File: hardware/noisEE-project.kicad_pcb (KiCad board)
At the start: 2 copper layers, 109.9 x 56.5 mm, 113 parts, among them IC1 ATTINY84-S, J1 VOL_CONN, J2 Stereo_CONN, J3 COLOR_CONN, J4 USB_OTG, M3 MountingHole_3.2mm_M3, P2 ISP_02x03, Q1 PN2222A, Q2 PN2222A, SW1 SW_DIP_x01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

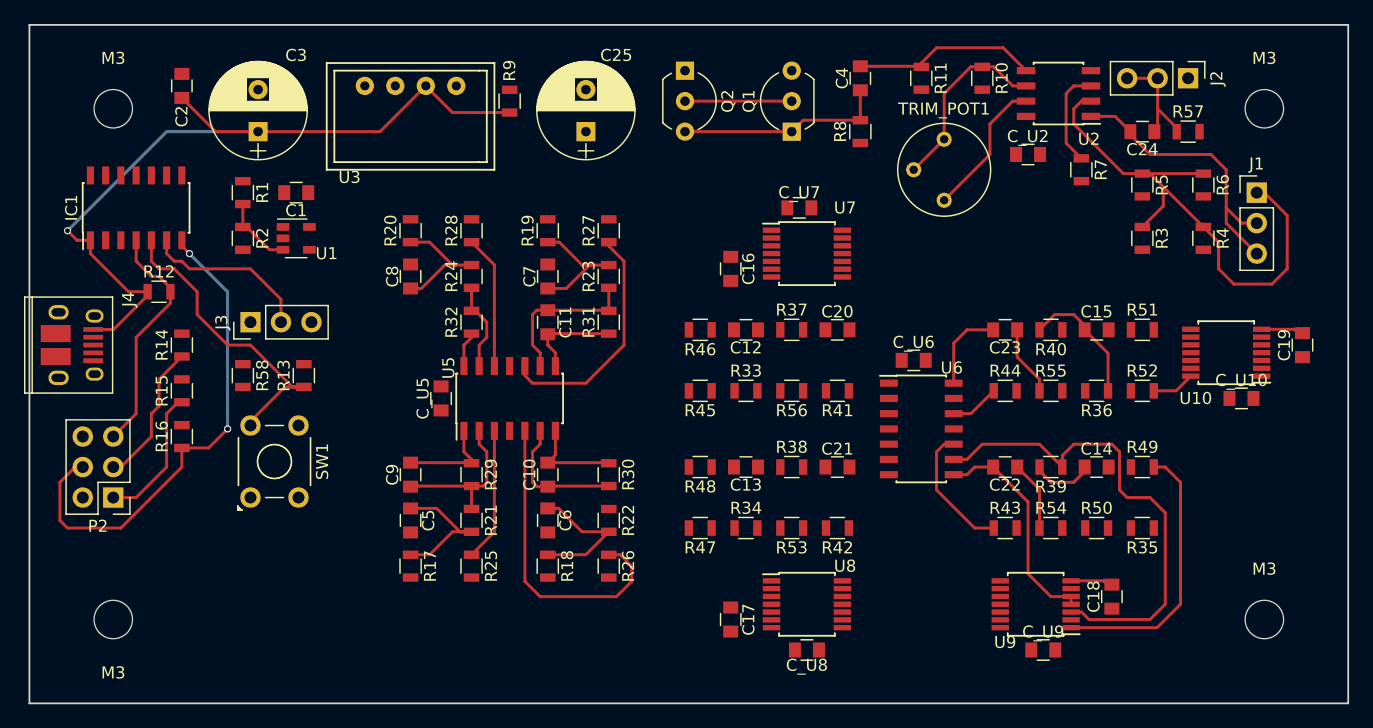
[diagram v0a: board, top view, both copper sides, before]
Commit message: Use two opamps for pre-amp and output stages, clean up board and lay down tracks for all signal paths
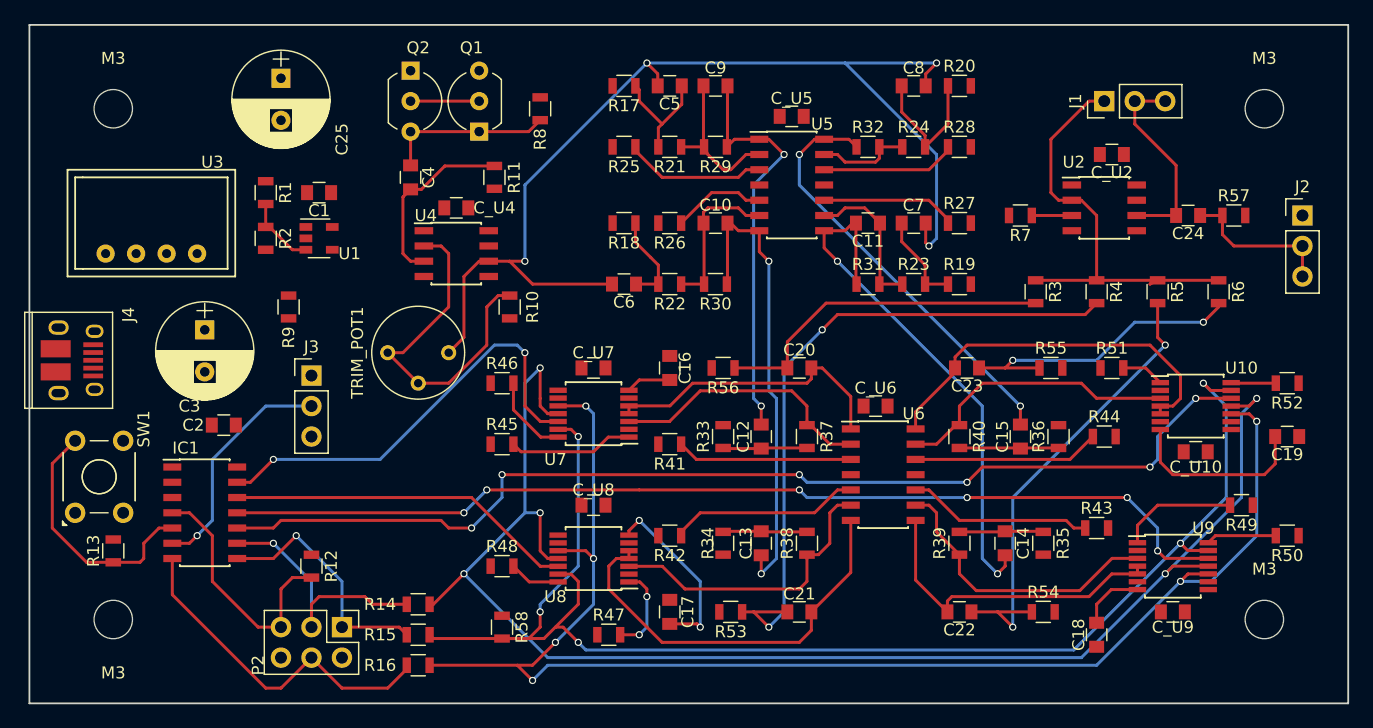
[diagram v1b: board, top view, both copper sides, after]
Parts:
- added C_U4: 0.1u, Capacitors_SMD:C_0805, F.Cu at (102.9, 74.9)
- added U4: OPA227, Housings_SOIC:SOIC-8_3.9x4.9mm_Pitch1.27mm, F.Cu at (102.9, 78.7)
- U2: value OPA2227 -> OPA227
- moved R20 47.3 mm to (144.8, 64.8), turned to 0 degrees
- moved C8 44.8 mm to (141.0, 64.8), turned to 0 degrees
- moved R17 43.8 mm to (116.8, 64.8), turned to 180 degrees
- moved R10 43.7 mm to (107.3, 83.2)
- moved TRIM_POT1 43.2 mm to (102.2, 87.0), turned to 90 degrees
- moved C5 42.1 mm to (120.7, 64.8), turned to 180 degrees
- moved R28 41.2 mm to (144.8, 69.8), turned to 0 degrees
- moved C9 41.2 mm to (124.5, 64.8), turned to 0 degrees
- moved R24 38.4 mm to (141.0, 69.8), turned to 0 degrees
- moved C4 38.4 mm to (99.1, 72.4), turned to 270 degrees
- moved C_U5 37.5 mm to (130.8, 67.3), turned to 0 degrees
- moved R25 37.2 mm to (116.8, 69.8), turned to 180 degrees
- moved R11 36.5 mm to (106.0, 72.4)
- moved R32 36.1 mm to (137.2, 69.8), turned to 0 degrees
- moved R21 35.2 mm to (120.7, 69.8), turned to 180 degrees
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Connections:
- U2 pad 1: Net-(C24-Pad2) -> Net-(U2-Pad1)
- U2 pad 5: Net-(C4-Pad2) -> Net-(U2-Pad5)
- U2 pad 6: Net-(R10-Pad1) -> Net-(C24-Pad2)
- U2 pad 7: Noise -> +9V
- U2 pad 8: +9V -> Net-(U2-Pad8)
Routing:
- net SPI_CLK: track 0.00 -> 123.0 mm, vias 0 -> 5
- net SPI_MOSI: track 0.00 -> 119.7 mm, vias 0 -> 6
- net SPI_MISO: track 0.00 -> 117.6 mm, vias 0 -> 5
- net SS_INFT: track 0.00 -> 90.6 mm, vias 0 -> 6
- net SS_5300: track 0.00 -> 85.2 mm, vias 0 -> 6
- net Noise: track 11.7 -> 91.9 mm, vias 0 -> 4
- net +5V: track 65.7 -> 0.00 mm, vias 1 -> 0
- net N_0270: track 0.00 -> 55.9 mm, vias 0 -> 2
- net SS_0016: track 0.00 -> 36.7 mm, vias 0 -> 2
- net Net-(C11-Pad2): track 8.01 -> 44.4 mm, vias 0 -> 2
- net W_0270: track 0.00 -> 34.1 mm
- net N_5300: track 5.85 -> 39.3 mm, vias 0 -> 2
- net Net-(C15-Pad2): track 2.96 -> 35.7 mm, vias 0 -> 2
- net Net-(C10-Pad2): track 8.01 -> 39.2 mm, vias 0 -> 2
- net SS_0270: track 0.00 -> 29.1 mm
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
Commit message: Laid down almost all tracks. GND and Earth seem to be treated as synonyms
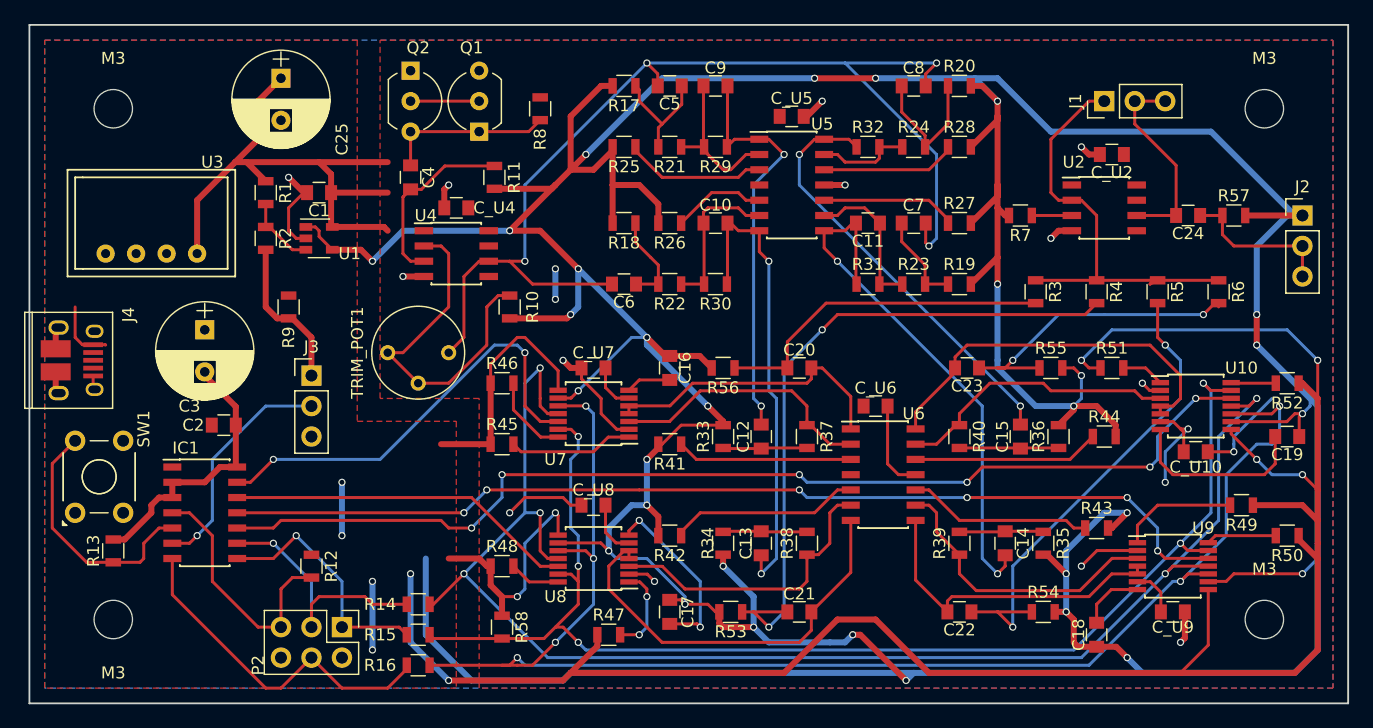
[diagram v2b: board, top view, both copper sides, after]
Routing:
- net GND: track 0.00 -> 476.3 mm, vias 0 -> 30
- net +5V: track 0.00 -> 212.5 mm, vias 0 -> 8
- net Earth: track 0.00 -> 103.0 mm, vias 0 -> 14
- net +9V: track 0.00 -> 70.1 mm, vias 0 -> 2
- net (no net): track 0.00 -> 12.7 mm, vias 0 -> 6
- net SPI_MISO: track 117.6 -> 108.4 mm
- net SPI_MOSI: track 119.7 -> 123.7 mm
- net N_5300: track 39.3 -> 40.4 mm
- net N_INFT: track 25.2 -> 26.0 mm
- added copper zone on F.Cu, net +5V
- added copper zone on F.Cu, net +9V
- added copper zone on B.Cu, net Earth

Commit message: Split up the ground (GND->VCOM)
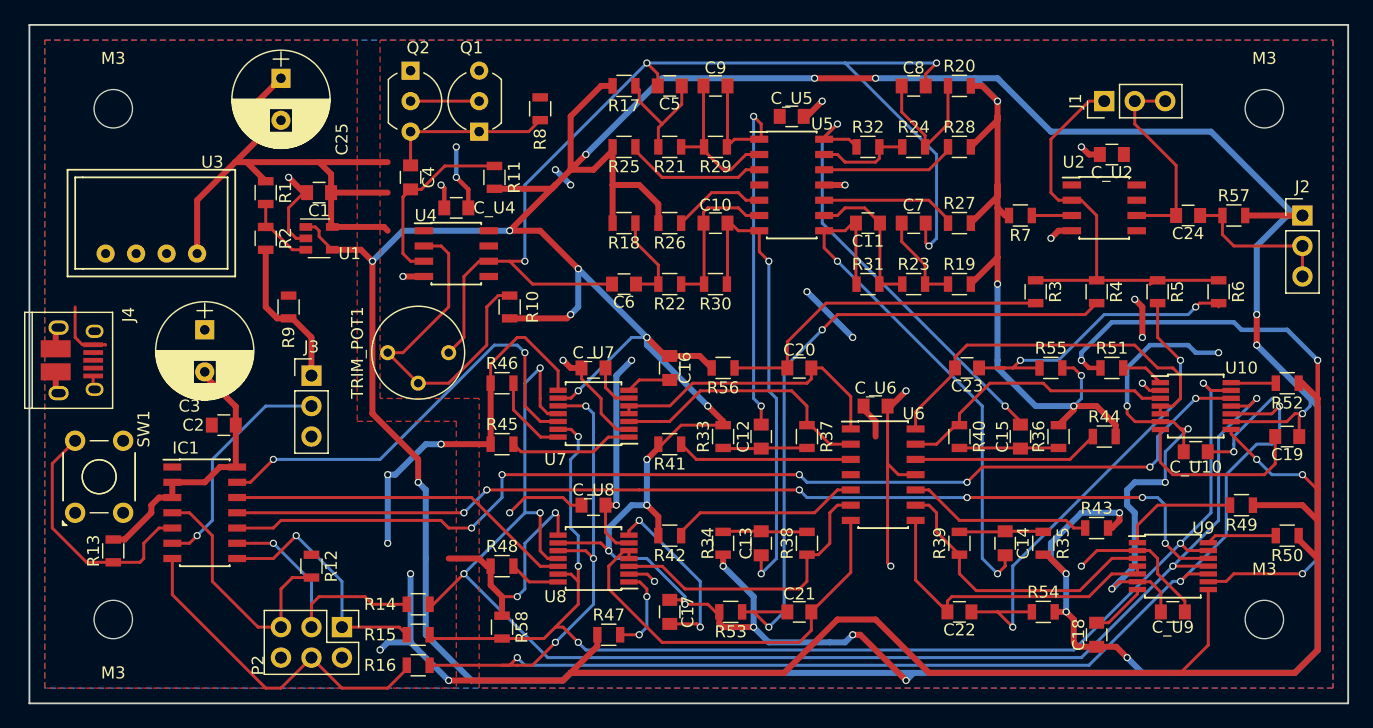
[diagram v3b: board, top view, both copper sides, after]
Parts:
- C4: value 1uF -> 1u
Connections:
- net GND renamed VCOM
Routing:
- net +9V: track 70.1 -> 129.8 mm, vias 2 -> 13
- net VCOM: track 476.3 -> 504.1 mm, vias 30 -> 31
- net Earth: track 103.0 -> 121.7 mm, vias 14 -> 17
- net +5V: track 212.5 -> 227.7 mm, vias 8 -> 12
- net (no net): track 12.7 -> 0.00 mm, vias 6 -> 0
- net Net-(C12-Pad2): track 35.1 -> 36.9 mm
- net Net-(C15-Pad2): track 35.7 -> 37.1 mm
- net SPI_CLK: track 123.0 -> 122.1 mm
- net SS_5300: track 85.2 -> 85.9 mm
- net Net-(C18-Pad2): track 5.45 -> 4.76 mm

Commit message: Get the plane stiches to stay in with hacky net bindings
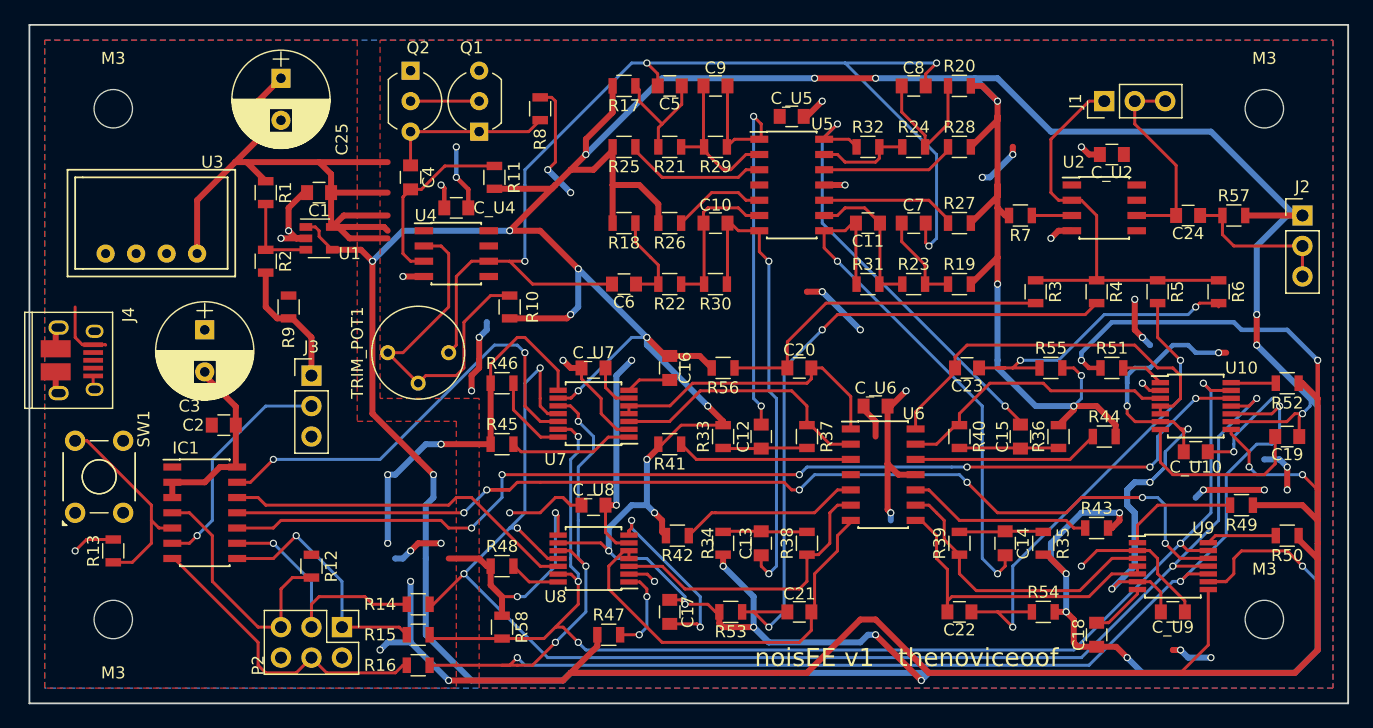
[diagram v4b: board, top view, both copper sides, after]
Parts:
- added A: plane_pad, NoisEE_Components:plane_pad, F.Cu at (97.8, 104.1)
- added B: plane_pad, NoisEE_Components:plane_pad, B.Cu at (170.2, 95.9)
- added C: plane_pad, NoisEE_Components:plane_pad, B.Cu at (164.5, 99.1)
- added D: plane_pad, NoisEE_Components:plane_pad, F.Cu at (149.2, 69.8)
- added X: plane_pad, NoisEE_Components:plane_pad, F.Cu at (132.1, 81.9)
- added Y: plane_pad, NoisEE_Components:plane_pad, F.Cu at (160.7, 86.4)
- added Z: plane_pad, NoisEE_Components:plane_pad, F.Cu at (105.4, 84.5)
- added e: plane_pad, NoisEE_Components:plane_pad, F.Cu at (162.6, 111.8)
- moved R2 1.91 mm to (87.0, 79.4)
- moved R42 0.63 mm to (121.3, 102.2)
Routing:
- net +9V: track 129.8 -> 168.4 mm, vias 13 -> 17
- net Earth: track 121.7 -> 140.2 mm, vias 17 -> 27
- net VCOM: track 504.1 -> 509.3 mm
- net SS_5300: track 85.9 -> 90.4 mm
- net TP_20: track 21.2 -> 17.6 mm
- net ISP_MOSI: track 28.8 -> 26.2 mm
- net Net-(J1-Pad1): track 36.9 -> 35.8 mm
- net Net-(R1-Pad2): track 6.04 -> 7.16 mm
- net SPI_CLK: track 122.1 -> 121.0 mm
- net Noise: track 91.9 -> 93.0 mm
- net Net-(R42-Pad1): track 15.9 -> 15.1 mm
- net SPI_MOSI: track 123.7 -> 123.1 mm
- net SS_INFT: track 90.6 -> 90.0 mm
- net SS_0270: track 29.1 -> 29.6 mm
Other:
- net class Default: clearance 0.25 -> 0.2
- rule trace_clearance: 0.25 -> 0.2

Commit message: Various tweaks: expanding some pours, moved the USB side mounting holes
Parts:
- moved M3 5.08 mm to (79.4, 66.7)
- moved M3 5.08 mm to (79.4, 109.2)
- moved J2 3.17 mm to (173.4, 72.4)
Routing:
- net VCOM: track 509.3 -> 511.7 mm
- net ISP_MOSI: track 26.2 -> 27.5 mm
- net Net-(C24-Pad1): track 13.0 -> 12.0 mm
- net ISP_RESET: track 21.3 -> 20.6 mm

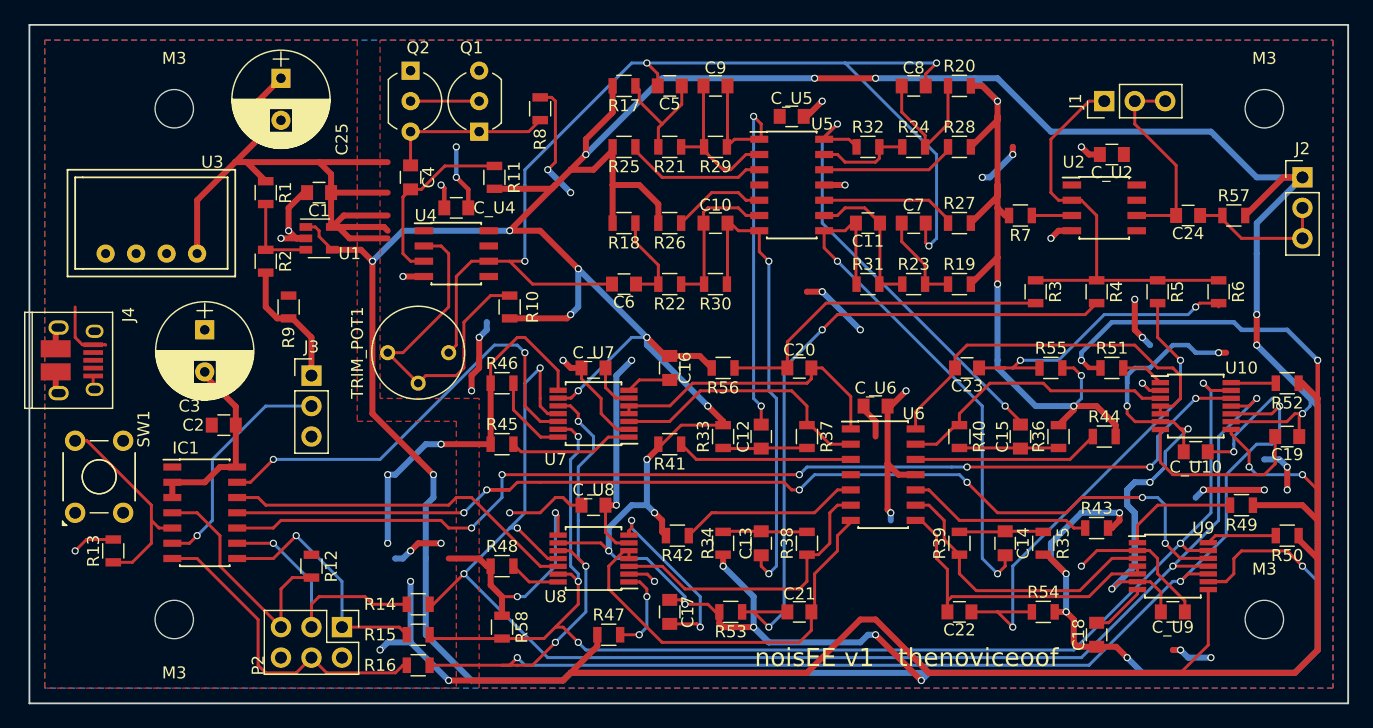
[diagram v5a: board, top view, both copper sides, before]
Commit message: Check in v2 hardware with fixes for USI and AD5292 Vss issues
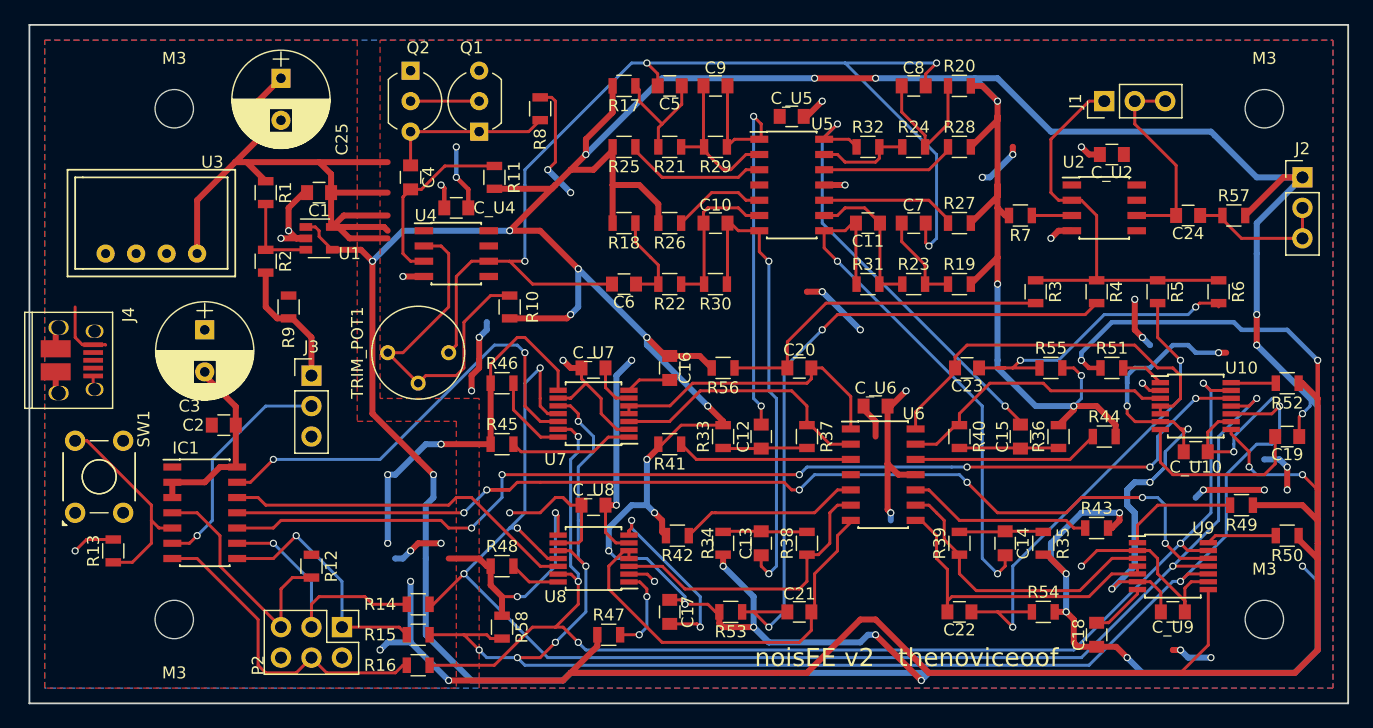
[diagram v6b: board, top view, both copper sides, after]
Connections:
- R15 pad 2: SPI_MISO -> SPI_MOSI
- R16 pad 2: SPI_MOSI -> SPI_MISO
- R58 pad 2: SPI_MISO -> SPI_MOSI
- U10 pad 9: VCOM -> Earth
- U7 pad 9: VCOM -> Earth
- U8 pad 9: VCOM -> Earth
- U9 pad 9: VCOM -> Earth
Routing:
- net VCOM: track 511.7 -> 479.8 mm, vias 31 -> 30
- net Earth: track 140.2 -> 156.1 mm
- net SPI_MOSI: track 123.1 -> 125.4 mm, vias 6 -> 7
- net SPI_MISO: track 108.4 -> 109.2 mm
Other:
- board text added: "noisEE v2 thenoviceoof"
- board text removed: "noisEE v1 thenoviceoof"
